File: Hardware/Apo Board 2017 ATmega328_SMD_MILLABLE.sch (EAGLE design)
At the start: 29 parts, among them U1 LED-TRICOLOR-5050-IC, U10 LED-TRICOLOR-5050-IC, U11 LED-TRICOLOR-5050-IC, U2 ATMEGA328P_PDIP, U3 LED-TRICOLOR-5050-IC, U4 LED-TRICOLOR-5050-IC, U5 LED-TRICOLOR-5050-IC, U6 LED-TRICOLOR-5050-IC, U7 LED-TRICOLOR-5050-IC, U8 LED-TRICOLOR-5050-IC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

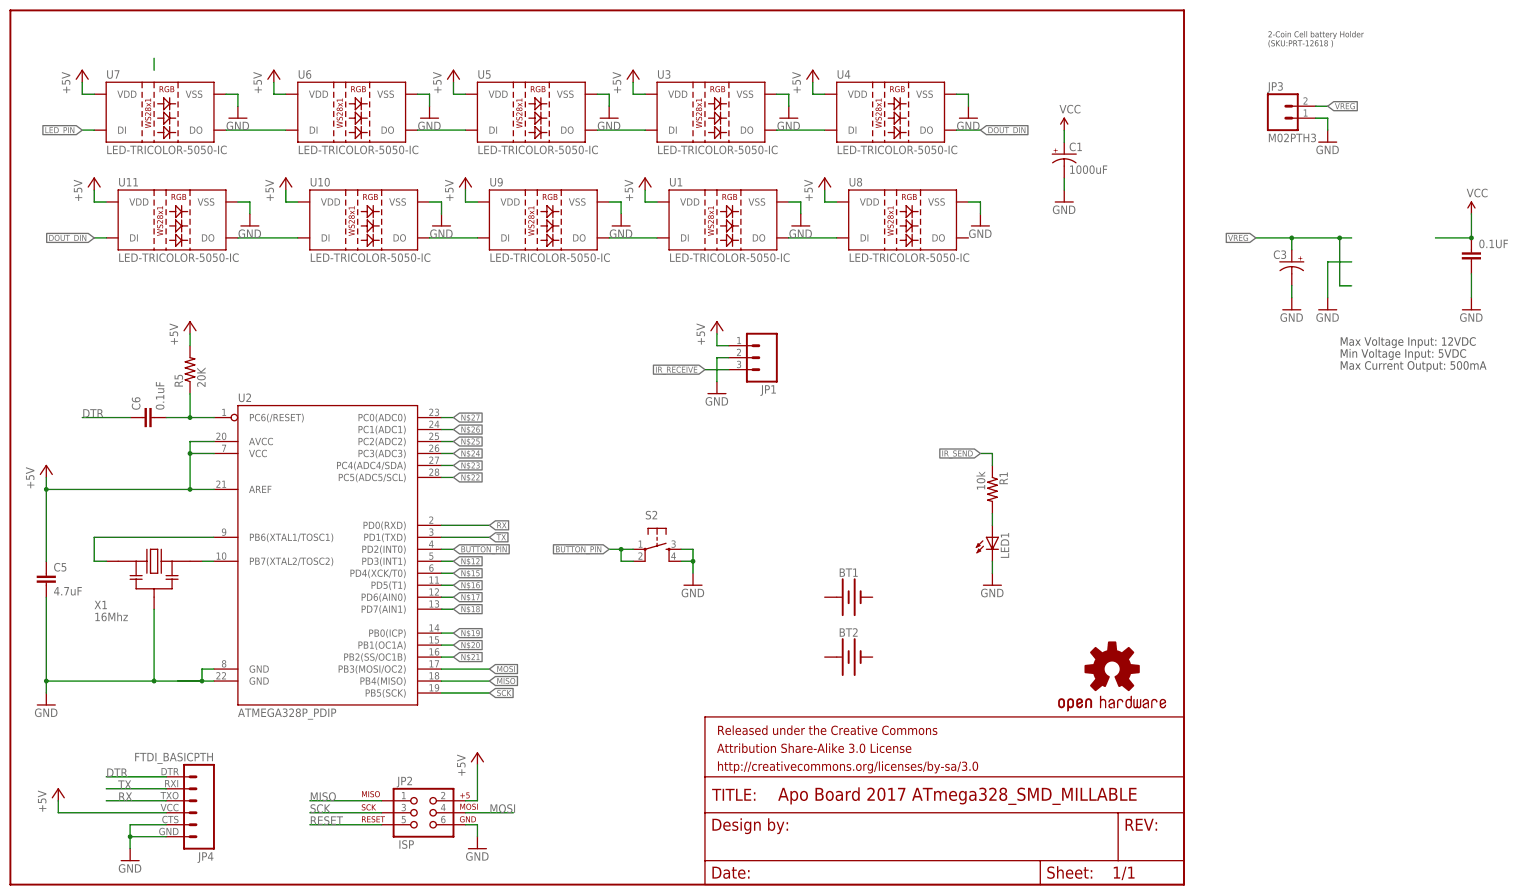
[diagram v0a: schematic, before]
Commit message: Adding ATmega328 versions
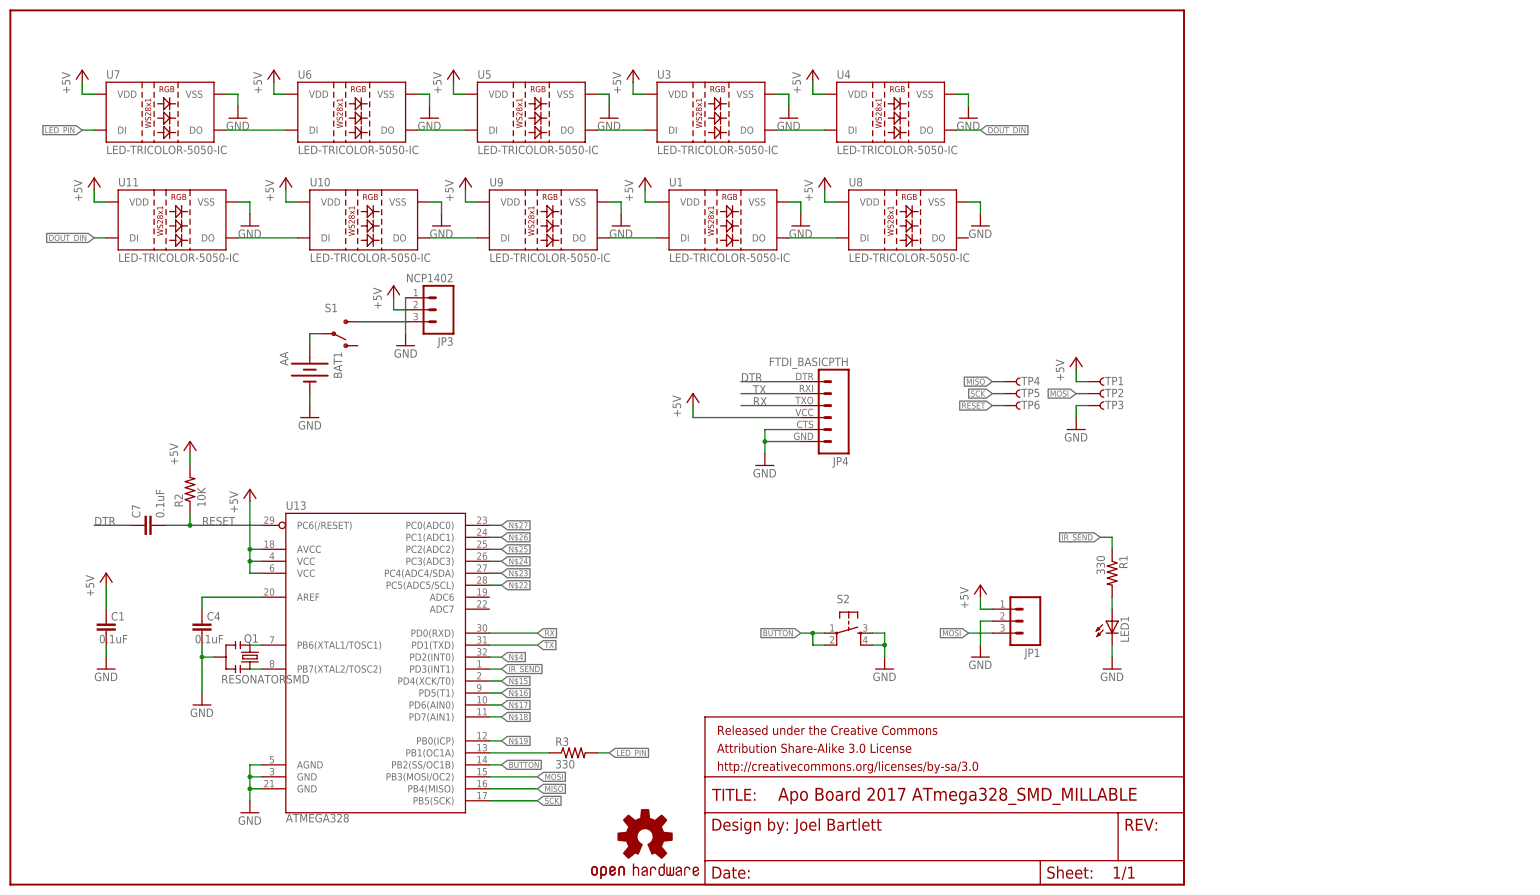
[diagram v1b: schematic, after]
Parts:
- removed 0.1UF: (no value), SparkFun-Capacitors:CAPKIT
- removed BT1, BT2: (no value), SparkFun-Batteries:BATTERY-AAA
- removed C3: (no value), SparkFun-Capacitors:CAP_POLPTH2
- removed C5: 4.7uF, SparkFun-Passives:CAPKIT
- removed C6: 0.1uF, SparkFun-Passives:CAPKIT
- removed JP2: ISP, SparkFun:AVR_SPI_PRG_6PTH
- removed R5: 20K, SparkFun-Passives:RESISTORKIT
- removed U2: ATMEGA328P_PDIP, SparkFun-DigitalIC:ATMEGA328P_PDIP
- removed X1: 16Mhz, 1_Dan Master:CERAMIC_RESONATOR
- added BAT1: AA, SparkFun:BATTERYAA-KIT
- added C4, C7: 0.1uF, SparkFun:CAP0402-CAP
- added Q1: RESONATORSMD, SparkFun:RESONATORSMD
- added R2: 10K, SparkFun:RESISTOR0402-RES
- added R3: 330, SparkFun-Resistors:RESISTORPTH-1/4W
- added S1: (no value), SparkFun:SWITCH-SPSTKIT
- added TP1, TP2, TP3, TP4, TP5, TP6: TP-3x5, SparkFun-Passives:TEST-POINT3X5
- added U13: ATMEGA328, SparkFun:ATMEGA168
- C1: value 1000uF -> 0.1uF; device SparkFun-Capacitors:CAP_POLPTH2 -> SparkFun:CAP0402-CAP
- JP1: device SparkFun-Connectors:M03PTH -> SparkFun-Connectors:M03IR_RECEIVER
- JP3: value M02PTH3 -> NCP1402; device SparkFun-Connectors:M02PTH3 -> SparkFun-Connectors:M03BOOST
- R1: value 10k -> 330
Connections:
- removed net BUTTON_PIN: S2.1, S2.2, U2.PD2(INT0)
- removed net IR_RECEIVE: JP1.3
- removed net N$10: C6.2, R5.1, U2.PC6(/RESET)
- removed net N$12: U2.PD3(INT1)
- removed net N$21: U2.PB2(SS/OC1B)
- removed net VCC: 0.1UF.1, C1.+
- removed net VREG: C3.+, JP3.2
- new net AREF: C4.2, U13.AREF
- new net BUTTON: S2.1, S2.2, U13.PB2(SS/OC1B)
- new net N$29: Q1.1, U13.PB7(XTAL2/TOSC2)
- new net N$30: Q1.3, U13.PB6(XTAL1/TOSC1)
- new net N$8: JP3.3, S1.S
- net +5V: now also C1.2, JP3.2, R2.2, TP1.1, U13.AVCC, U13.VCC@1, U13.VCC@2; no longer C5.1, JP2.2, R5.2, U2.AREF, U2.AVCC, U2.VCC
- net DTR: now also C7.1; no longer C6.1
- net GND: now also BAT1.-, C1.1, C4.1, Q1.2, TP3.1, U13.AGND, U13.GND@1, U13.GND@2; no longer 0.1UF.2, C1.-, C3.-, C5.2, JP2.6, U2.GND@1, U2.GND@2, X1.P$2
- net IR_SEND: now also U13.PD3(INT1)
- net LED_PIN: now also R3.2
- net MISO: now also TP4.1, U13.PB4(MISO); no longer JP2.1, U2.PB4(MISO)
- net MOSI: now also JP1.3, TP2.1, U13.PB3(MOSI/OC2); no longer JP2.4, U2.PB3(MOSI/OC2)
- net N$15: now also U13.PD4(XCK/T0); no longer U2.PD4(XCK/T0)
- net N$16: now also U13.PD5(T1); no longer U2.PD5(T1)
- net N$17: now also U13.PD6(AIN0); no longer U2.PD6(AIN0)
- net N$18: now also U13.PD7(AIN1); no longer U2.PD7(AIN1)
- net N$19: now also U13.PB0(ICP); no longer U2.PB0(ICP)
- net N$20: now also R3.1, U13.PB1(OC1A); no longer U2.PB1(OC1A)
- net N$22: now also U13.PC5(ADC5/SCL); no longer U2.PC5(ADC5/SCL)
- net N$23: now also U13.PC4(ADC4/SDA); no longer U2.PC4(ADC4/SDA)
- net N$24: now also U13.PC3(ADC3); no longer U2.PC3(ADC3)
- net N$25: now also U13.PC2(ADC2); no longer U2.PC2(ADC2)
- net N$26: now also U13.PC1(ADC1); no longer U2.PC1(ADC1)
- net N$27: now also U13.PC0(ADC0); no longer U2.PC0(ADC0)
- net N$4: now also U13.PD2(INT0); no longer U2.PB6(XTAL1/TOSC1), X1.P$1
- net N$7: now also BAT1.+, S1.P; no longer U2.PB7(XTAL2/TOSC2), X1.P$3
- net RESET: now also C7.2, R2.1, TP6.1, U13.PC6(/RESET); no longer JP2.5
- net RX: now also U13.PD0(RXD); no longer U2.PD0(RXD)
- net SCK: now also TP5.1, U13.PB5(SCK); no longer JP2.3, U2.PB5(SCK)
- net TX: now also U13.PD1(TXD); no longer U2.PD1(TXD)
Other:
- note added: "Joel Bartlett"
- note removed: "2-Coin Cell battery Holder (SKU:PRT-12618 )"
- note removed: "Max Current Output: 500mA"
- note removed: "Max Voltage Input: 12VDC"
- note removed: "Min Voltage Input: 5VDC"
- moved on the sheet: JP1, JP4, LED1, R1, S2
